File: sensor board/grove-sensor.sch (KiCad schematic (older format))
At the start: 43 parts, among them P1 CONN_01X03, P2 CONN_01X06, P3 CONN_01X03, P4 CONN_01X07, P5 CONN_01X01, P6 CONN_01X01, Q1 Q_NPN_BEC, U1 ADD8704, U2 SI1143, U3 Teensy_3.1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

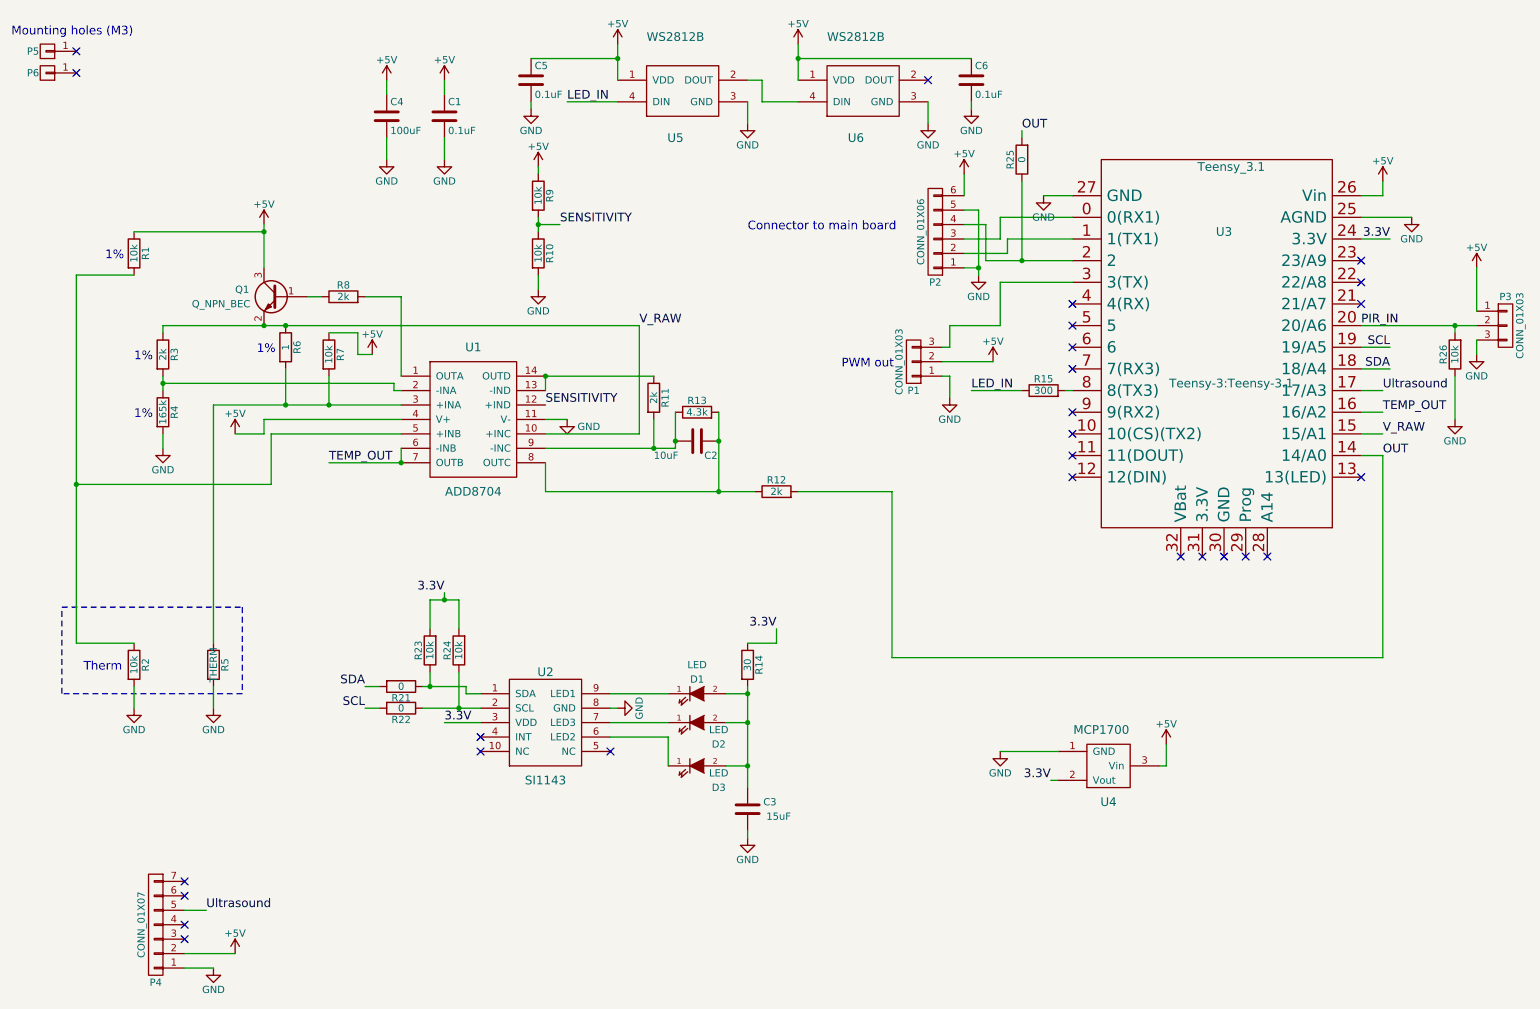
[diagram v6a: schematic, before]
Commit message: Various changes:
* Ultrasonic doesn't reset PIR timeout
* Probably fix led black issue
* Open flower at start and then close slowly
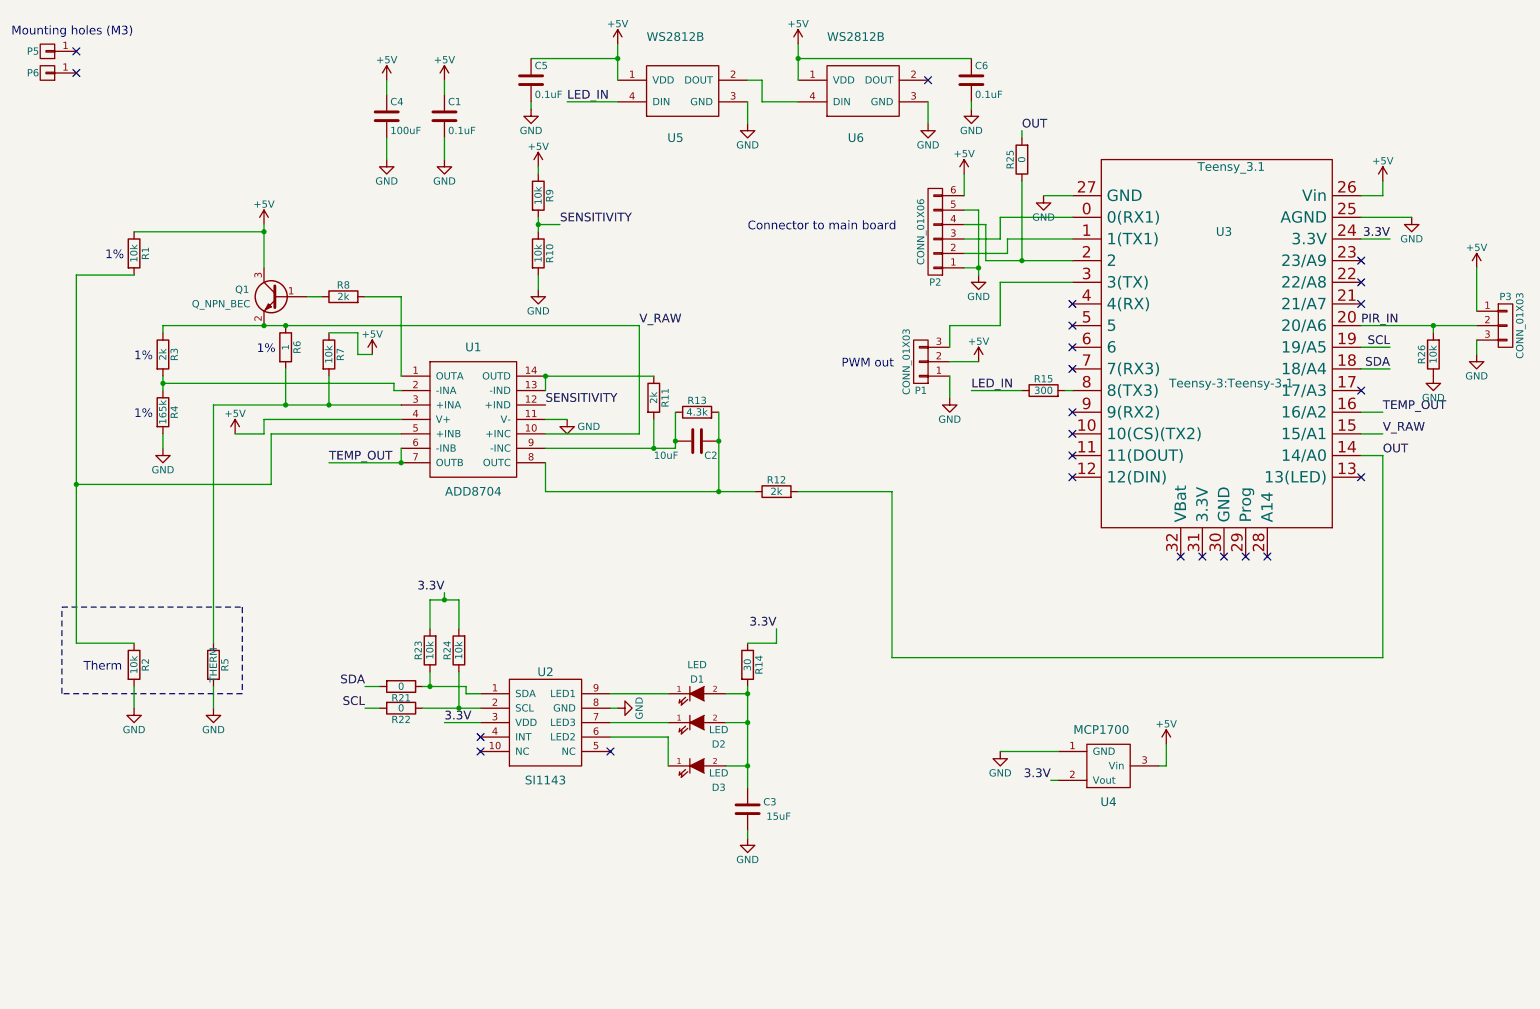
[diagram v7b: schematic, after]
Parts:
- removed P4: CONN_01X07, Pin_Headers:Pin_Header_Straight_1x07, symbol CONN_01X07
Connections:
- net Ultrasound: no longer names the net of U3.17 (17/A3)
- no-connect marks 27 -> 24
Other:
- moved on the sheet: P1, R26
